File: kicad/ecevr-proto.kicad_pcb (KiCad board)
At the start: 4 copper layers, 100 x 100 mm, 220 parts, among them J19 SFP, J20 SFP_CAGE, J2001 IO_CONN, J2201 BEL_0845_2G1T_H5, J3 USB_C_Receptacle_USB2.0, J4 JTAG, J5 LSHM-150-04_JB1, J6 LSHM-150-04_JB2, Q1 SSM6N35AFE, Q2 SSM6N35AFE, Q3 Si3477, Q4 SSM6N35AFE, Q5 SSM6N35AFE, SW1 PROG, SW2101 SW_DIP_x08, U10 74LVC1G06, U12 5P49V6965, U13 TPS3808DBV, U14 74LVC1G06, U17 74LVC06, U18 74LVC1T126, U2001 74LVC2T45DC, U21 74LVC1G06, U2101 74AHC1T86, U2102 74AHC1T86, U2103 PCA9306, U2104 24FC16T, U2105 74AHC1T86, U2106 74AHC1T86, U2201 74AHC1T86, U2202 74LVC1G06, U2301 lan9254, U8 74ALVC125, U9 TLV62569ADDC, X2301 FNETHE025, Y1 25MHz

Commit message: basic layout done
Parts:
- moved H8 53.5 mm to (128.5, 64.0)
- moved H6 22.5 mm to (176.8, 93.8)
- moved U14 20.4 mm to (125.7, 48.6)
- moved Q1 9.98 mm to (159.5, 33.1)
- moved R76 8.54 mm to (129.3, 75.5), turned to -90 degrees
- moved R2106 4.06 mm to (161.1, 89.4), turned to -90 degrees
- moved R26 1.07 mm to (155.3, 80.4), turned to -90 degrees
- moved R31 1.04 mm to (156.8, 80.4), turned to 90 degrees
- moved R2114 0.87 mm to (167.9, 86.9), turned to 180 degrees
- moved R2104 0.57 mm to (162.6, 89.4)
- moved JP2201 0.46 mm to (160.3, 46.0)
- moved U2202 0.40 mm to (168.6, 45.5)
- moved U2105 0.35 mm to (168.1, 89.3)
- moved R62 0.12 mm to (128.5, 78.1)
- turned R32 to 0 degrees
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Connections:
- Q1 pad 1: IO_L9P_34 -> IO_L3P_34
- Q1 pad 4: IO_L9N_34 -> IO_L3N_34
- Q2 pad 5: /power/POWER_CYCLE -> IO_L14N_34
- Q5 pad 2: /LEDs/LED8 -> IO_L9N_34
- Q5 pad 5: /LEDs/LED7 -> IO_L9P_34
- R2 pad 2: SDA0 -> IO_L19N_34
- R2002 pad 1: IO_L20P_15 -> IO_L11P_34
- R2108 pad 2: /lan9254/EEP_SZ -> IO_L12N_34
- R2112 pad 1: /lan9254/I2C_ISOLb -> IO_L21P_34
- R2113 pad 2: /lan9254/I2C_ISOLb -> IO_L21P_34
- R2115 pad 1: /lan9254/EEP_WP -> IO_L19P_34
- R2116 pad 1: /lan9254/EEP_SZ -> IO_L12N_34
- R2117 pad 1: /lan9254/EEP_SZ -> IO_L12N_34
- R64 pad 1: IO_L9P_34 -> IO_L3P_34
- R65 pad 1: IO_L9N_34 -> IO_L3N_34
- R72 pad 2: SCL0 -> IO_L21N_34
- R79 pad 1: /power/POWER_CYCLE -> IO_L14N_34
- R92 pad 1: /SFP Connector/PRESENTb -> IO_L2P_34
- R93 pad 2: /SFP Connector/PRESENTb -> IO_L2P_34
- R94 pad 1: /SFP Connector/LOS -> IO_L2N_34
- R95 pad 2: /SFP Connector/LOS -> IO_L2N_34
- R96 pad 1: /SFP Connector/TX_FAULT -> IO_L1P_34
- R97 pad 2: /SFP Connector/TX_FAULT -> IO_L1P_34
- SW2101 pad 10: /lan9254/JP7 -> IO_L11N_34
- SW2101 pad 15: /lan9254/I2C_ISOLb -> IO_L21P_34
- SW2101 pad 9: /lan9254/JP8 -> IO_L20P_15
- U12 pad 8: IO_L9N_34 -> IO_L3N_34
- U12 pad 9: IO_L9P_34 -> IO_L3P_34
- U17 pad 1: /LEDs/LED6 -> IO_L24N_34
- U17 pad 11: /LEDs/LED2 -> IO_L18N_34
- U17 pad 13: /LEDs/LED3 -> IO_L20P_34
- U17 pad 3: /LEDs/LED5 -> IO_L20N_34
- U17 pad 5: /LEDs/LED4 -> IO_L18P_34
- U17 pad 9: /LEDs/LED1 -> IO_L16P_34
- U2001 pad 5: IO_L20P_15 -> IO_L11P_34
- U21 pad 1: Net-(U21-Pad1) -> IO_L1N_34
- U21 pad 2: Net-(U21-Pad1) -> IO_L1N_34
- U2102 pad 1: /lan9254/EEP_SZ -> IO_L12N_34
- U2103 pad 5: SDA0 -> IO_L19N_34
- U2103 pad 6: SCL0 -> IO_L21N_34
- U2104 pad 1: SCL0 -> IO_L21N_34
- U2104 pad 3: SDA0 -> IO_L19N_34
- U2104 pad 5: /lan9254/EEP_WP -> IO_L19P_34
- U2105 pad 4: /lan9254/EEP_SZ -> IO_L12N_34
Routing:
- net IO_L12N_34: track 0.00 -> 76.5 mm, vias 0 -> 2
- net IO_L3N_34: track 0.00 -> 73.1 mm, vias 0 -> 3
- net IO_L3P_34: track 0.00 -> 72.2 mm, vias 0 -> 2
- net Net-(D7-BK): track 6.42 -> 68.3 mm
- net IO_L11P_34: track 0.00 -> 60.9 mm
- net IO_L14N_15: track 10.3 -> 61.3 mm, vias 0 -> 2
- net IO_L13P_15: track 9.79 -> 60.3 mm, vias 0 -> 2
- net IO_L14P_15: track 11.1 -> 61.5 mm, vias 0 -> 2
- net IO_L22N_15: track 11.6 -> 61.0 mm, vias 0 -> 2
- net IO_L3P_15: track 10.7 -> 60.0 mm, vias 2 -> 3
- net IO_L22P_15: track 12.5 -> 61.8 mm, vias 0 -> 2
- net IO_L13N_15: track 0.00 -> 49.1 mm, vias 0 -> 2
- net Net-(D8-RK): track 3.84 -> 49.0 mm
- net IO_L12N_15: track 0.00 -> 44.7 mm, vias 0 -> 2
- net IO_L20N_15: track 1.33 -> 46.0 mm, vias 0 -> 2
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- removed copper zone on In2.Cu, net +5V
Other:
- board size 100 x 100 mm -> 86.3 x 69.7 mm
- board text added: "EtherCat EVR V2.0.0"
- board text removed: "EtherCat EVR V1.1.0"
- board text removed: "ON"
- board text removed: "REF 1V8"

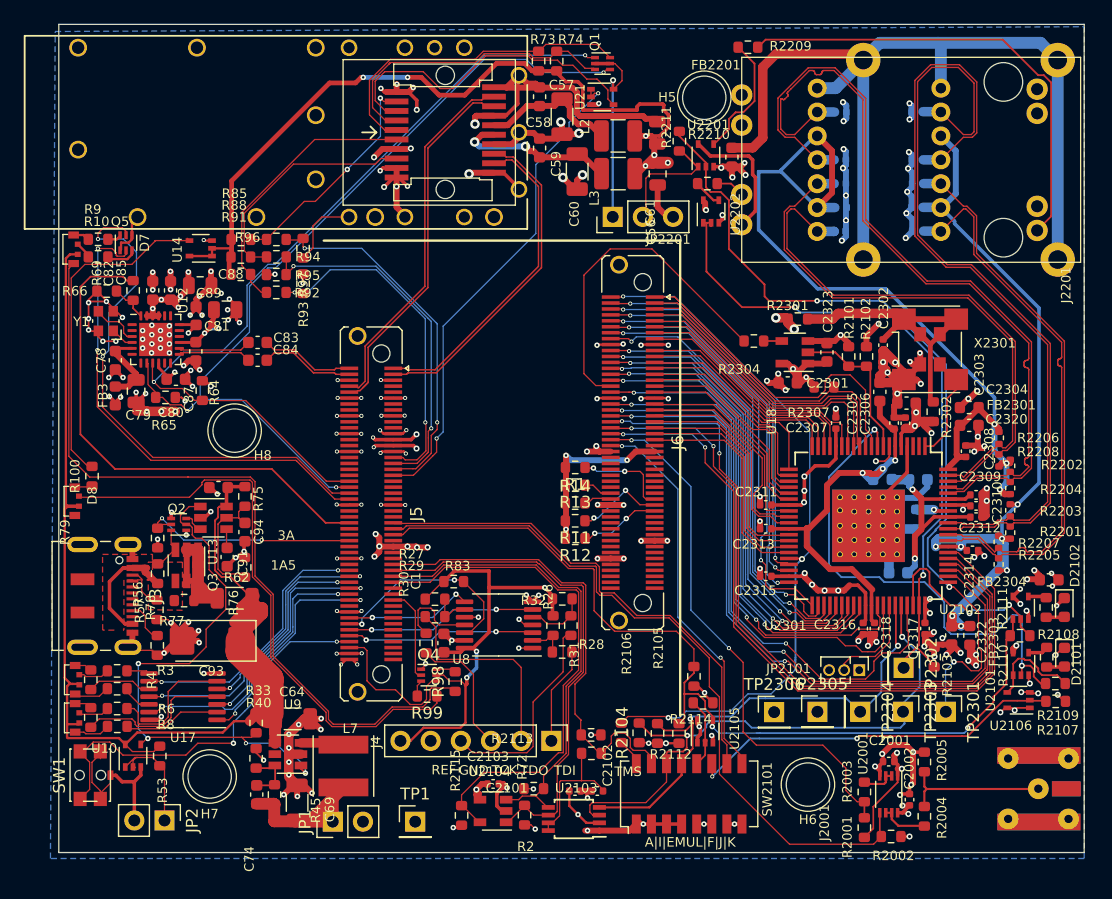
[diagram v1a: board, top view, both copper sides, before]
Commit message: First stab. Connected power, added holes and frst clean of silk.
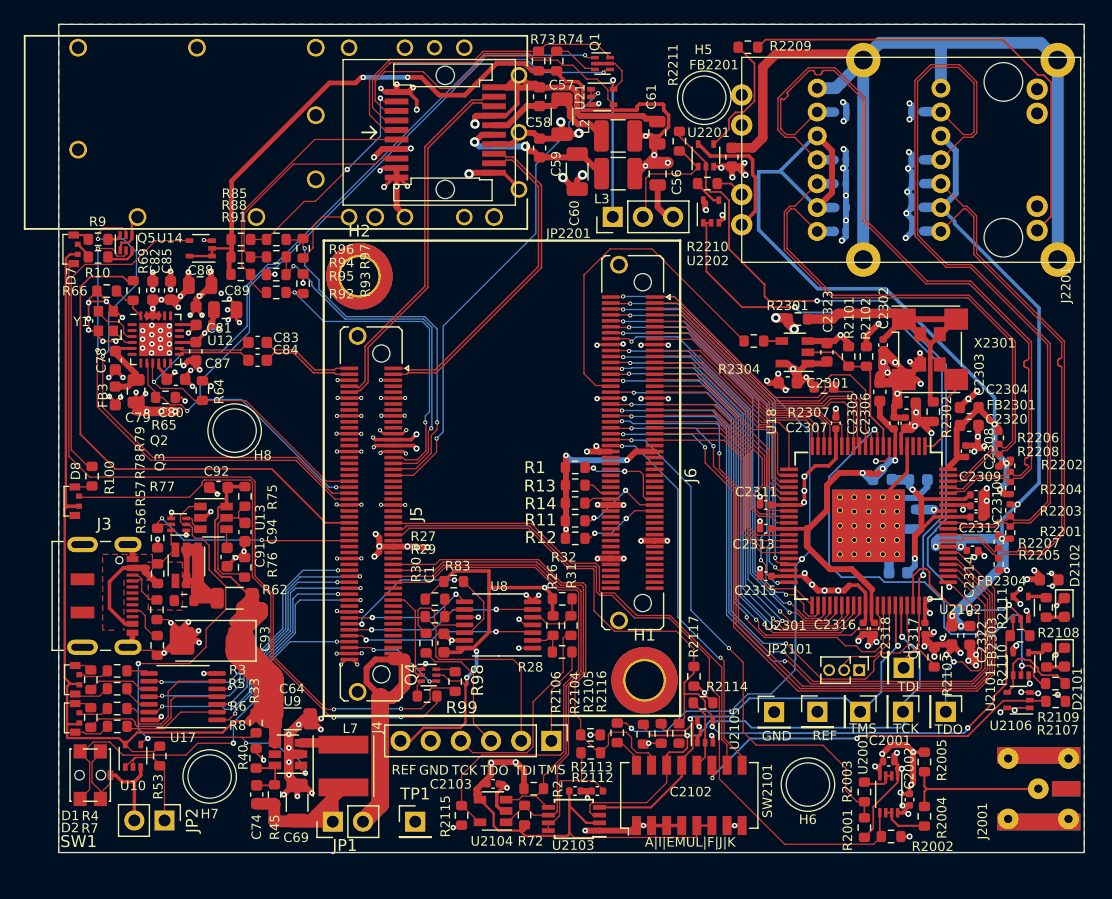
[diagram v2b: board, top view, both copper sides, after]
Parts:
- added H1: MountingHole_Pad, MountingHole:MountingHole_3.2mm_M3_DIN965_Pad_TopBottom, F.Cu at (163.0, 85.0)
- added H2: MountingHole_Pad, MountingHole:MountingHole_3.2mm_M3_DIN965_Pad_TopBottom, F.Cu at (139.0, 51.0)
- moved R2104 0.36 mm to (162.9, 89.5)
- moved R2106 0.35 mm to (160.7, 89.4)
- moved R2105 0.31 mm to (164.4, 89.5)
- moved SW2101 0.13 mm to (166.8, 94.7)
- moved R2112 0.07 mm to (158.5, 91.1)
- moved R2113 0.05 mm to (158.4, 89.6)
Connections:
- J2001 pad 3: (no net) -> unconnected-(J2001-Ext-Pad3)
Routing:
- net +3V3: track 123.3 -> 206.4 mm
- net +1V8: track 115.2 -> 142.3 mm, vias 50 -> 46
- net /CFG_DONE: track 12.3 -> 8.47 mm, vias 0 -> 2
- net /VCCIO_0: track 62.5 -> 59.9 mm
- net MGT_TX3_N: track 31.5 -> 29.6 mm
- net Net-(D7-BK): track 68.3 -> 66.4 mm, vias 0 -> 2
- net /lan9254/EESCL: track 49.9 -> 48.4 mm
- net MGT_TX3_P: track 30.9 -> 29.6 mm
- net /lan9254/LINKACT1: track 57.3 -> 56.1 mm
- net Net-(D8-RK): track 49.0 -> 47.9 mm, vias 0 -> 2
- net Net-(JP2201-C): track 10.3 -> 9.33 mm
- net IO_L1P_34: track 30.9 -> 31.9 mm
- net IO_L13P_15: track 60.3 -> 59.3 mm
- net IO_L19P_34: track 44.1 -> 45.0 mm
- net /SFP Connector/TX_DISABLE: track 28.0 -> 27.1 mm
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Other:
- board text removed: "1A5"
- board text removed: "3A"

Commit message: further work; will need to redo vias :-( for jlcpcb
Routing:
- net GND: track 346.2 -> 342.4 mm
- net +1V8: track 142.3 -> 144.9 mm
- net IO_L2P_34: track 28.7 -> 27.6 mm
- net IO_L21P_34: track 40.2 -> 39.4 mm

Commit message: prepared for JLCPCB; created gerbers
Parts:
- moved C78 0.20 mm to (118.5, 58.3)
- moved FB3 0.20 mm to (118.5, 61.3)
- moved R99 0.17 mm to (144.7, 86.5)
- moved R2105 0.12 mm to (164.3, 89.5)
- moved R2116 0.12 mm to (165.8, 89.5)
- moved R2104 0.12 mm to (162.8, 89.6)
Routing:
- net IO_L24N_34: track 19.6 -> 17.7 mm
- net IO_L20N_34: track 19.5 -> 17.6 mm
- net IO_L18P_34: track 18.9 -> 17.1 mm
- net /SFP Connector/TX_DISABLE: track 27.1 -> 28.2 mm
- net /CFG_DONE: track 8.47 -> 9.53 mm
- net IO_L18N_34: track 23.1 -> 23.8 mm
- net GND: vias 213 -> 212
- net +3V3: track 206.4 -> 206.3 mm, vias 25 -> 24
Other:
- rule pad_to_mask_clearance: 0.048 -> 0

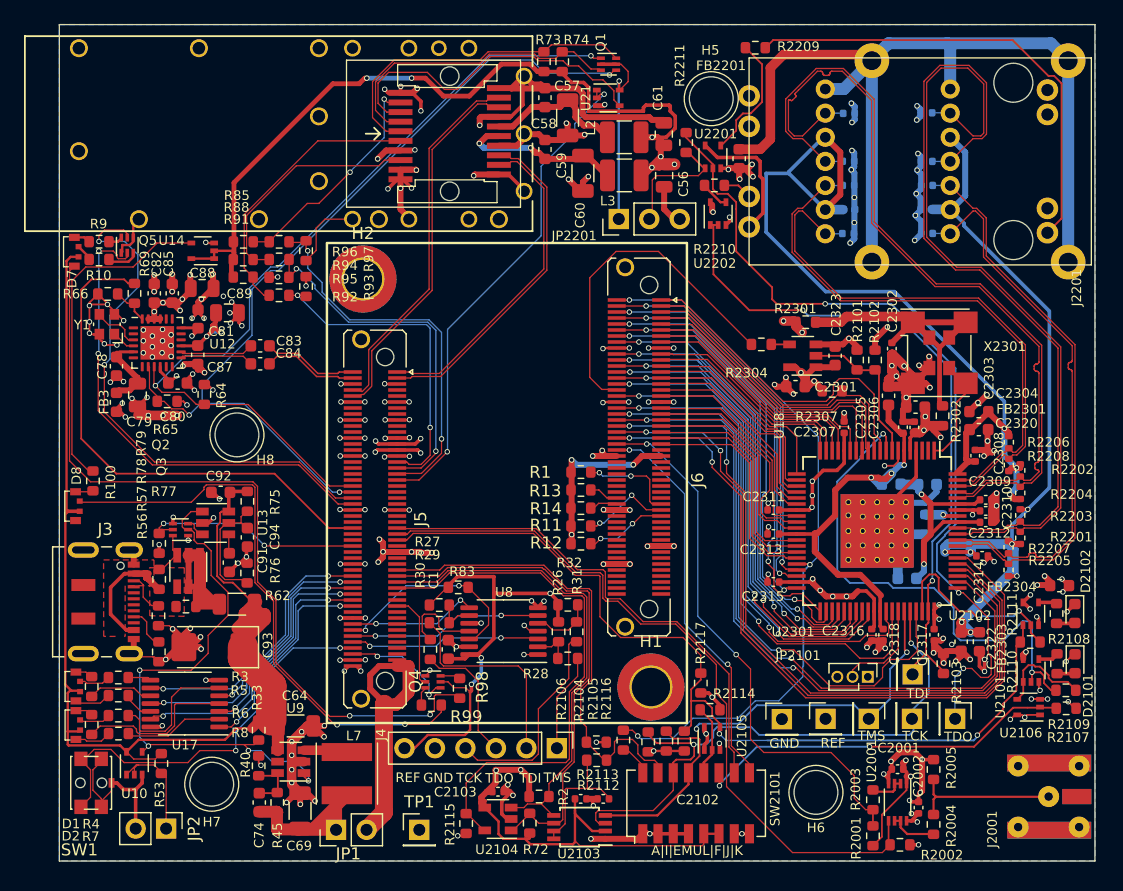
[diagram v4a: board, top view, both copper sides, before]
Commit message: JLC rework; originally submitted version was rejected
-> New rule, for 0.1mm min track-track sep the plane must be filled >30%
with copper. Fill front-plane but created carve-out for MGT diff-pairs.
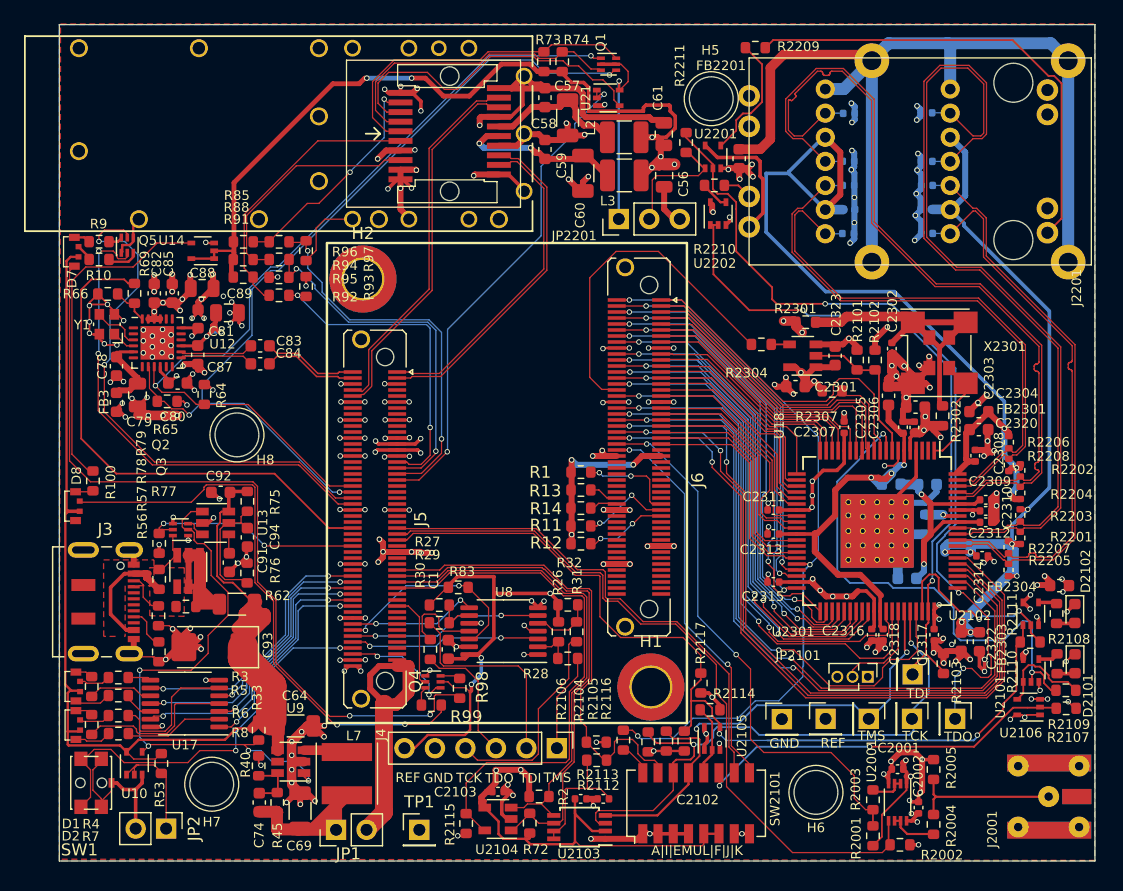
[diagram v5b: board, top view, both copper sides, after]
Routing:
- added copper zone on F.Cu, net GND
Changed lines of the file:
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@@
+    )
+  )
+  (zone (net 0) (net_name "") (layer "F.Cu") (hatch edge 0.508)
+    (connect_pads yes (clearance 0))
+    (min_thickness 0.125) (filled_areas_thickness no)
+    (keepout (tracks allowed) (vias allowed) (pads allowed) (copperpour not_allowed) (footprints allowed))
+    (fill (thermal_gap 0.508) (thermal_bridge_width 0.508))
+    (polygon
+      (pts
+        (xy 137.15 61)
+        (xy 135.1 61)
+        (xy 133.35 59.2)
+        (xy 123.25 59.2)
+        (xy 123.25 55.3)
+        (xy 134.3 55.3)
+        (xy 135.8 57.1)
+        (xy 138 54.9)
+        (xy 141.1 48.45)
+        (xy 141.05 40.45)
+        (xy 147.85 33.95)
+        (xy 152.65 33.95)
+        (xy 152.65 38.8)
+        (xy 157 42.9)
+        (xy 157 52.6)
+        (xy 149.1 60.95)
+      )
+    )
+  )
+  (zone (net 62) (net_name "GND") (layer "F.Cu") (hatch edge 0.508)
+    (connect_pads yes (clearance 0.125))
+    (min_thickness 0.2) (filled_areas_thickness no)
+    (fill yes (thermal_gap 0.508) (thermal_bridge_width 0.508))
+    (polygon
+      (pts
+        (xy 200 99.45)
+        (xy 113.7 99.35)
+        (xy 113.8 29.75)
+        (xy 200 29.75)
+      )
     )
   )
